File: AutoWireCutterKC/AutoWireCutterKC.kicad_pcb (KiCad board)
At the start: 2 copper layers, 59.7 x 38.1 mm, 20 parts, among them J1 LCD I/O, J2 ISP, J3 LCD, J5 Servo, J8 Barrel_Jack, J9 Stepper, M1 Conn_01x01_Male, M2 Conn_01x01_Male, M3 Conn_01x01_Male, M4 Conn_01x01_Male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

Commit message: Work on PCB layout
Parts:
- moved C6 20.1 mm to (136.1, 101.6), turned to 90 degrees
- moved U2 1.14 mm to (133.1, 77.2)
- moved U3 0.51 mm to (146.1, 79.5)
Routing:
- net GND: track 0.00 -> 43.2 mm
- net Net-(J1-Pad4): track 0.00 -> 29.7 mm, vias 0 -> 1
- net Net-(J1-Pad6): track 0.00 -> 29.6 mm, vias 0 -> 1
- net Net-(J1-Pad5): track 0.00 -> 27.3 mm, vias 0 -> 1
- net Net-(A1-Pad16): track 0.00 -> 23.6 mm
- net GNDREF: track 0.00 -> 23.2 mm, vias 0 -> 2
- net Net-(A1-Pad15): track 0.00 -> 21.7 mm
- net Net-(D1-Pad2): track 0.00 -> 19.8 mm, vias 0 -> 1
- net Net-(J1-Pad8): track 0.00 -> 19.6 mm, vias 0 -> 1
- net Net-(J1-Pad7): track 0.00 -> 16.7 mm, vias 0 -> 1
- net Net-(J2-Pad5): track 0.00 -> 14.7 mm, vias 0 -> 2
- net +5VL: track 0.00 -> 13.6 mm, vias 0 -> 2
- net Net-(J1-Pad2): track 0.00 -> 10.2 mm
- net Net-(A1-Pad3): track 0.00 -> 8.95 mm
- net Net-(A1-Pad4): track 0.00 -> 8.73 mm
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
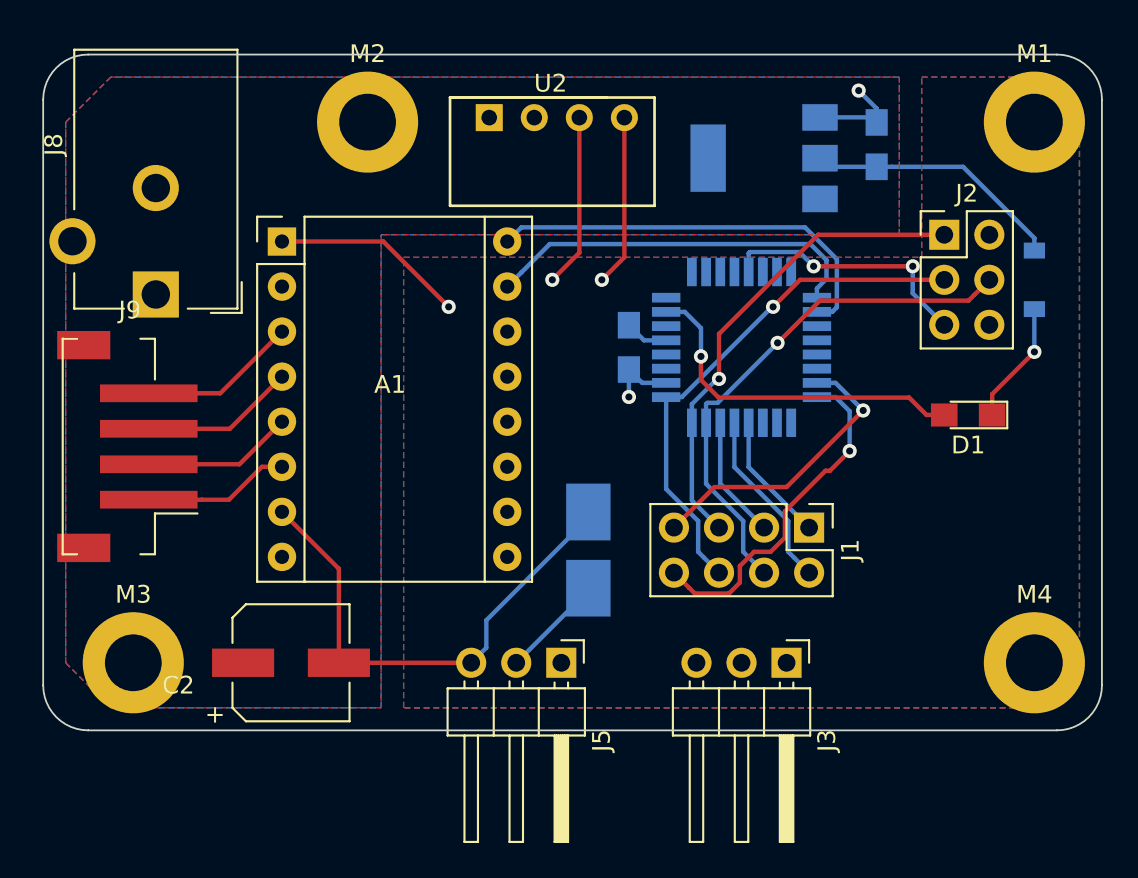
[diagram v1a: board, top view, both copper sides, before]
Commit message: Reworked Libraries
Fixed bug involving stepper not rotating. Taking things out of ISR helped. Servo wasn't responding because of incorrect DDRD register
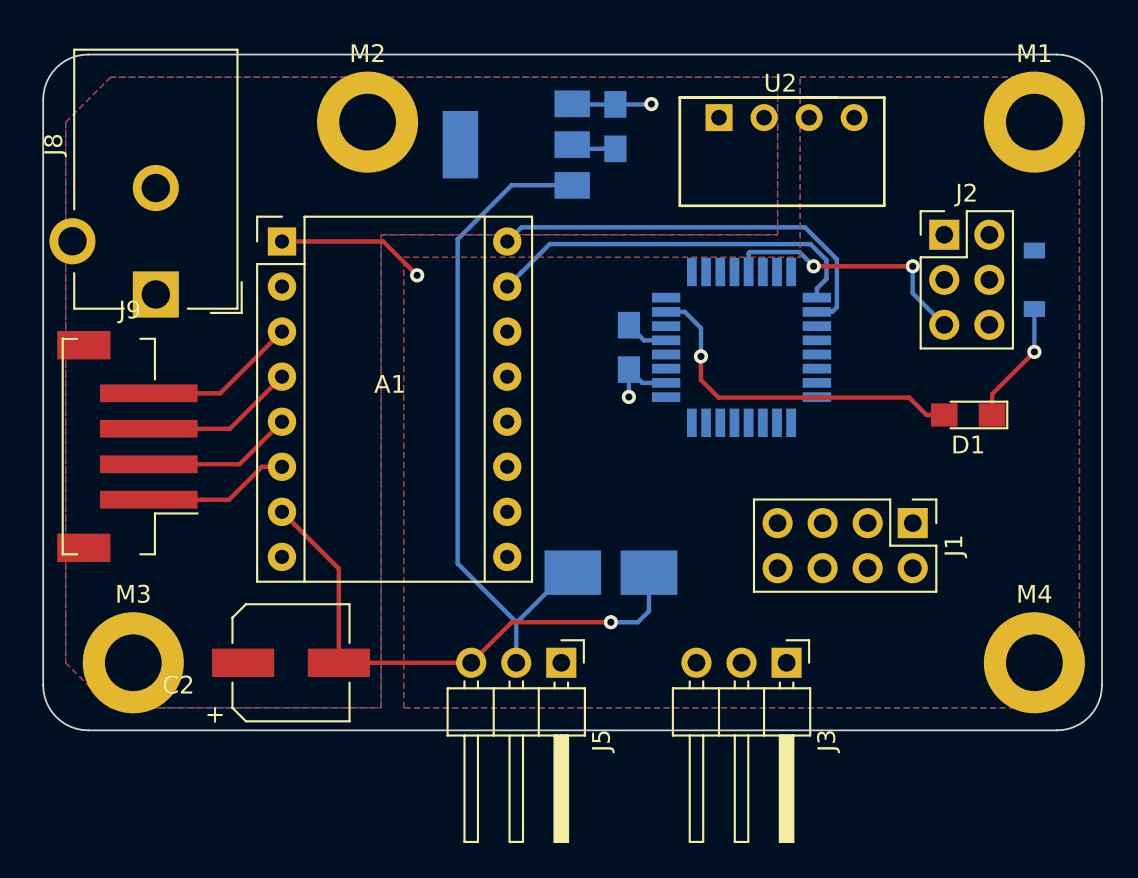
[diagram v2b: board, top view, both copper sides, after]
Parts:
- moved C5 14.8 mm to (137.7, 77.7)
- moved U3 14.0 mm to (132.1, 78.7)
- moved U2 13.0 mm to (146.1, 77.2)
- moved J1 5.85 mm to (154.4, 100.1)
- moved C6 1.80 mm to (137.4, 102.9), turned to 0 degrees
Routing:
- net +5V: track 5.88 -> 37.3 mm
- net Net-(J1-Pad4): track 29.7 -> 0.00 mm, vias 1 -> 0
- net Net-(J1-Pad6): track 29.6 -> 0.00 mm, vias 1 -> 0
- net Net-(J1-Pad5): track 27.3 -> 0.00 mm, vias 1 -> 0
- net Net-(J1-Pad8): track 19.6 -> 0.00 mm, vias 1 -> 0
- net Net-(J1-Pad7): track 16.7 -> 0.00 mm, vias 1 -> 0
- net GNDREF: track 23.2 -> 10.9 mm, vias 2 -> 1
- net Net-(J1-Pad2): track 10.2 -> 0.00 mm
- net GND: track 43.2 -> 33.2 mm, vias 0 -> 1
- net +5VL: track 13.6 -> 3.95 mm, vias 2 -> 1
- net Net-(J1-Pad1): track 7.32 -> 0.00 mm
- net Net-(J1-Pad3): track 6.93 -> 0.00 mm
- net +12V: track 5.54 -> 4.49 mm
